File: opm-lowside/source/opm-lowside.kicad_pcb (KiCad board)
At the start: 2 copper layers, 82 parts, among them IC1 INA180A3IDBVR, IC2 INA180A3IDBVR, IC3 INA180A3IDBVR, IC4 TMC6100-LA, J1 Current Sensing, J2 SPI/Info, J3 VCC_IO, J4 PWMx6, J5 Temperature, Q1 HYG025N06LS1C2, Q2 HYG025N06LS1C2, Q3 HYG025N06LS1C2, Q4 HYG025N06LS1C2, Q5 HYG025N06LS1C2, Q6 HYG025N06LS1C2, U1 TerminalBlock_2_P5.08mm, U2 TerminalBlock_3_P5.08mm

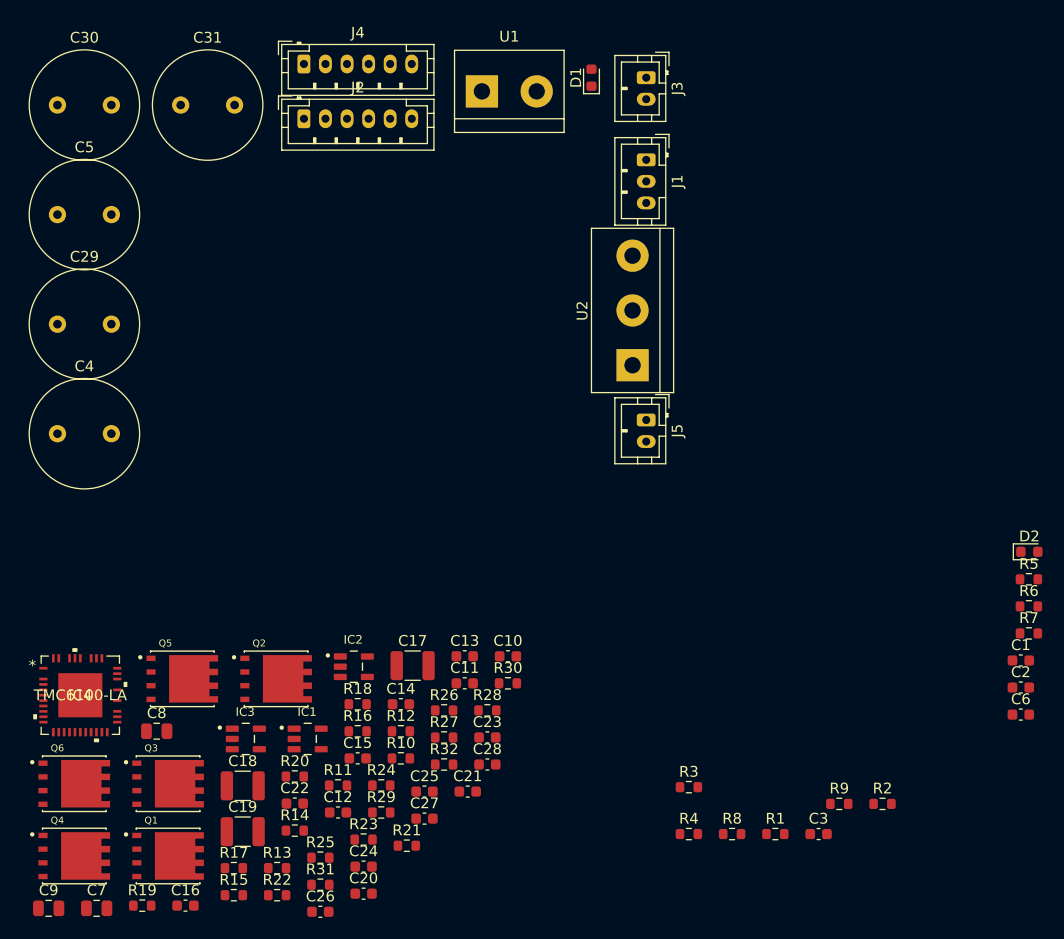
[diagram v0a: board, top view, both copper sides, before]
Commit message: add heatsink
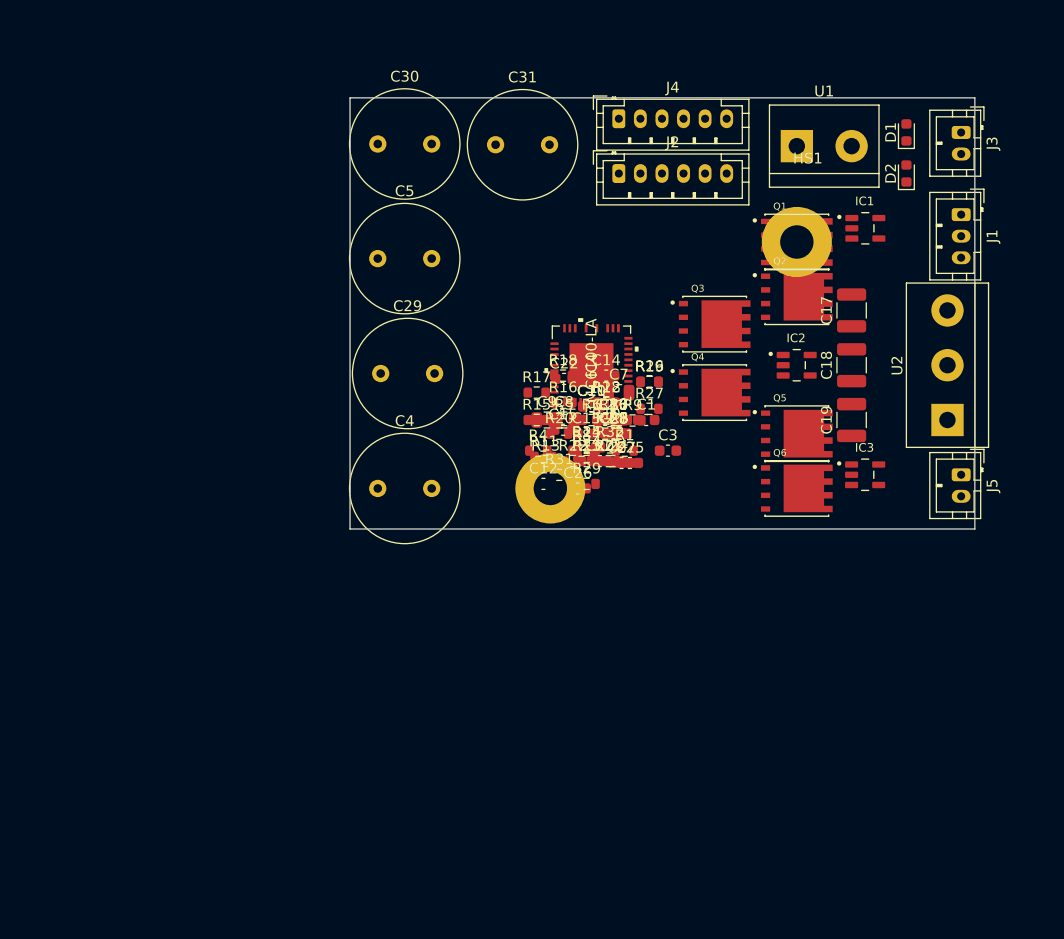
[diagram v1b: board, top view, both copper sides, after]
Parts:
- added HS1: Heatsink, Libraries:Heatsink_30x30mm_2xFixation3mm, F.Cu at (144.8, 106.7)
- moved Q1 81.5 mm to (171.4, 80.0)
- moved Q4 73.3 mm to (163.8, 94.0)
- moved Q6 72.4 mm to (171.4, 102.9)
- moved IC1 70.1 mm to (177.8, 78.7)
- moved C18 68.6 mm to (176.5, 91.4), turned to 90 degrees
- moved C19 68.2 mm to (176.5, 96.5), turned to 90 degrees
- moved C7 68.1 mm to (154.9, 94.0)
- moved R19 67.6 mm to (157.8, 93.0)
- moved Q3 66.2 mm to (163.8, 87.6)
- moved C9 64.7 mm to (148.3, 96.5)
- moved IC3 62.5 mm to (177.8, 101.6)
- moved Q5 61.4 mm to (171.4, 97.8)
- moved C16 60.0 mm to (154.4, 96.5)
- moved Q2 59.9 mm to (171.4, 85.1)
- moved IC4 56.4 mm to (152.4, 91.4), turned to 90 degrees
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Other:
- board outline added: 58 x 40 mm

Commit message: add step
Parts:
- IC4: value TMC6100-LA -> QFN37_7X7_TRI
- moved HS1 73.7 mm to (218.4, 105.4)
- moved C26 37.7 mm to (181.1, 80.0)
- moved C24 35.1 mm to (181.1, 77.5)
- moved R30 32.1 mm to (181.2, 78.7)
- moved C20 31.1 mm to (177.8, 81.3)
- moved C22 30.7 mm to (177.8, 105.4)
- moved R24 29.7 mm to (174.0, 80.0)
- moved R21 29.4 mm to (174.0, 78.7)
- moved R25 29.0 mm to (174.8, 81.3)
- moved R18 28.5 mm to (174.0, 77.5)
- moved C28 27.9 mm to (181.6, 104.1)
- moved R32 27.8 mm to (181.6, 102.9)
- moved C23 27.6 mm to (181.6, 101.6)
- moved R31 26.2 mm to (173.5, 91.4)
- moved R20 24.7 mm to (174.0, 100.3)
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
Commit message: update parts
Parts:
- C17: value 2,2μF/100V -> 2.2μF/100V
- IC4: value QFN37_7X7_TRI -> TMC6100-LA
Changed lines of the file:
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@@
       (effects (font (size 1 1) (thickness 0.15)))
     )
-    (fp_text value 2,2μF/100V (at 0 2.3 90) (layer F.Fab)
+    (fp_text value 2.2μF/100V (at 0 2.3 90) (layer F.Fab)
       (effects (font (size 1 1) (thickness 0.15)))
     )
@@
       (effects (font (size 1 1) (thickness 0.15)))
     )
-    (fp_text value QFN37_7X7_TRI (at 0 0 90) (layer F.SilkS)
-      (effects (font (size 1 1) (thickness 0.15)))
-    )
+    (fp_text value TMC6100-LA (at 0 0 90) (layer F.SilkS)
+      (effects (font (size 1 1) (thickness 0.15)))
+    )

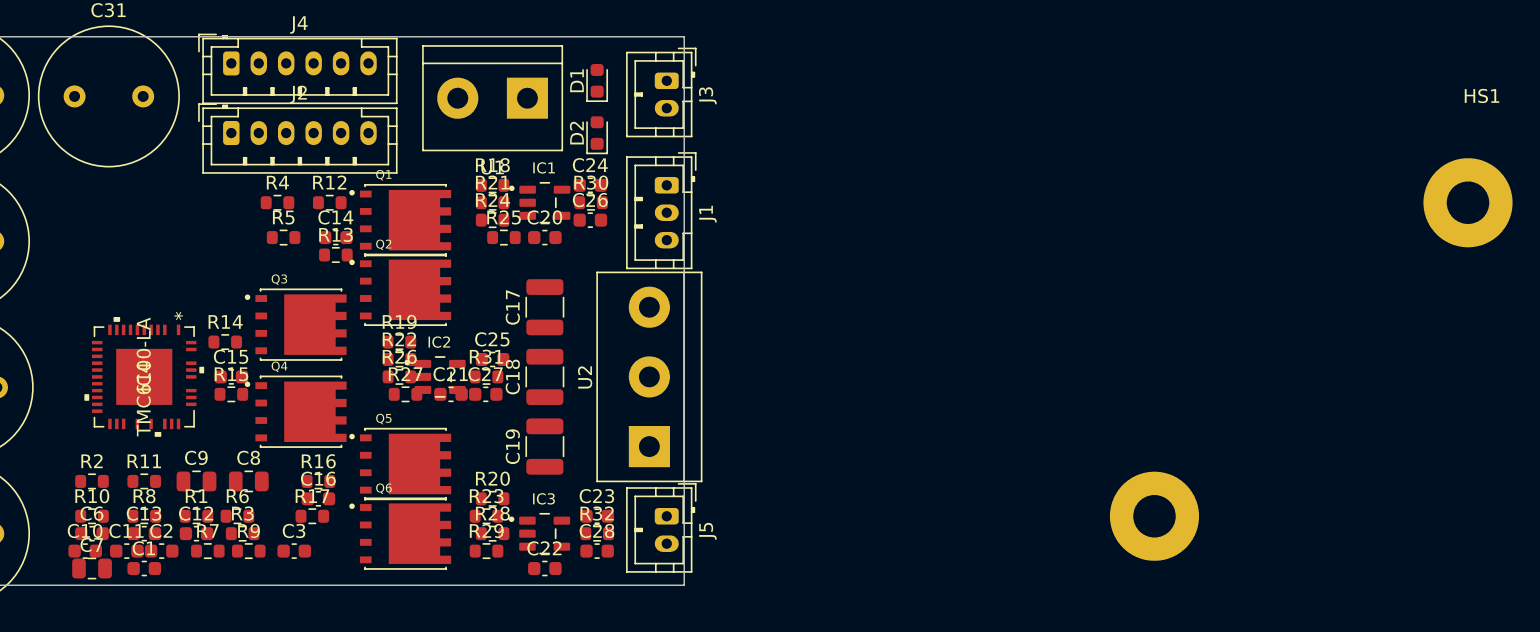
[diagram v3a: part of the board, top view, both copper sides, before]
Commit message: add fan
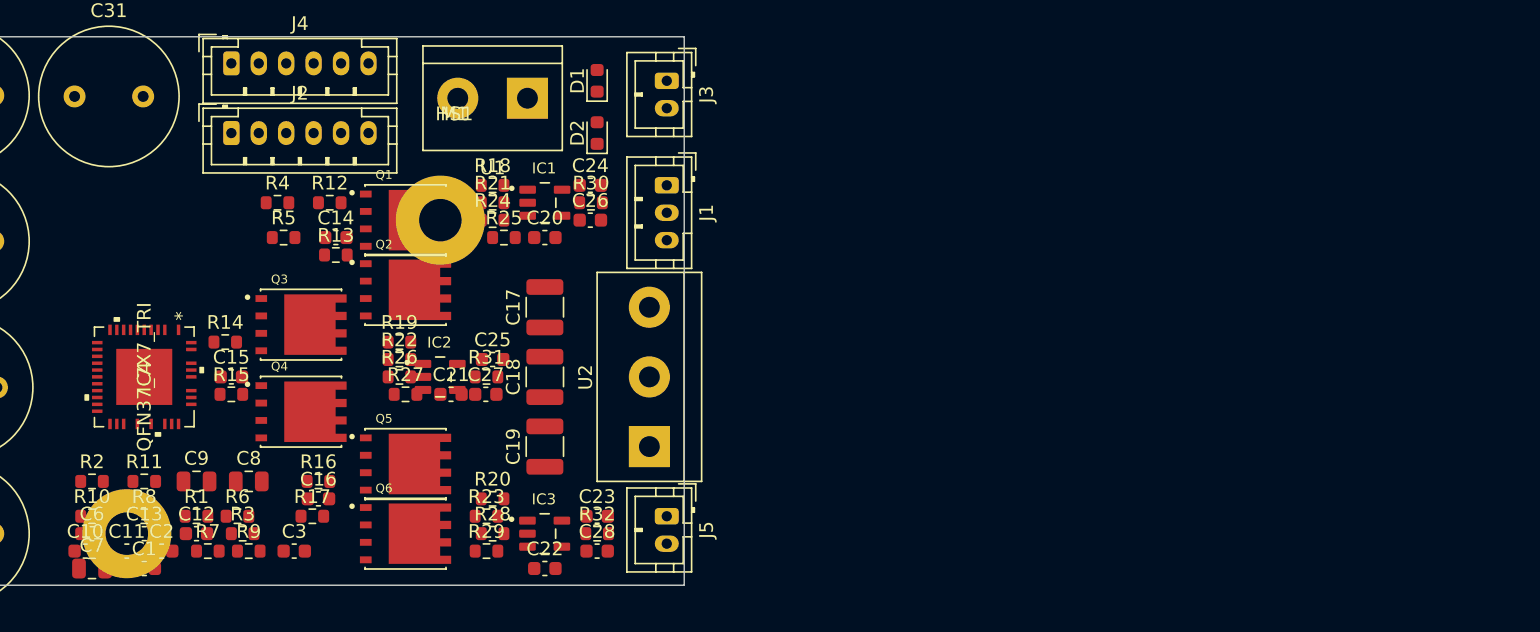
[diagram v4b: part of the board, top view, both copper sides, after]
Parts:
- added M1: Fan, Libraries:Fan_3010, F.Cu at (143.5, 106.7)
- IC4: value TMC6100-LA -> QFN37_7X7_TRI
- moved HS1 74.9 mm to (143.5, 106.7)
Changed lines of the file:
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@@
     (tracks 0)
     (zones 0)
-    (modules 83)
+    (modules 84)
     (nets 83)
   )
@@
       (effects (font (size 1 1) (thickness 0.15)))
     )
-    (fp_text value TMC6100-LA (at 0 0 90) (layer F.SilkS)
+    (fp_text value QFN37_7X7_TRI (at 0 0 90) (layer F.SilkS)
       (effects (font (size 1 1) (thickness 0.15)))
     )
@@
   )
   (module Libraries:Heatsink_30x30mm_2xFixation3mm (layer F.Cu)
-    (at 218.44 105.41)
+    (at 143.51 106.68)
     (descr "Heatsink, 62 x 40mm, 2x 3mm Drills,")
     (tags heatsink)
@@
     )
   )
+  (module Libraries:Fan_3010 (layer F.Cu)
+    (at 143.51 106.68)
+    (descr "fan 3010")
+    (tags heatsink)
+    (fp_text reference M1 (at 27.686 -34.417) (layer F.SilkS)
+      (effects (font (size 1 1) (thickness 0.15)))
+    )
+    (fp_text value Fan (at 11.43 -3.81) (layer F.Fab)
+      (effects (font (size 1 1) (thickness 0.15)))
+    )
+    (fp_arc (start 1.422977 -28.380326) (end 1.422977 -29.880326) (angle -90) (layer Dwgs.User) (width 0.2))
+    (fp_arc (start 1.422977 -1.680326) (end 0.562977 -1.680326) (angle -90) (layer Dwgs.User) (width 0.2))
+    (fp_arc (start 28.122977 -1.680326) (end 28.122977 -0.180326) (angle -90) (layer Dwgs.User) (width 0.2))
+    (fp_arc (start 1.422977 -1.680326) (end -0.077023 -1.680326) (angle -90) (layer Dwgs.User) (width 0.2))
+    (fp_arc (start 28.122977 -1.680326) (end 28.122977 -0.820326) (angle -90) (layer Dwgs.User) (width 0.2))
+    (fp_arc (start 1.422977 -28.380326) (end 1.422977 -29.240326) (angle -90) (layer Dwgs.User) (width 0.2))
+    (fp_arc (start 28.122977 -28.380326) (end 28.982977 -28.380326) (angle -90) (layer Dwgs.User) (width 0.2))
+    (fp_arc (start 28.122977 -28.380326) (end 29.622977 -28.380326) (angle -90) (layer Dwgs.User) (width 0.2))
+    (fp_circle (center 26.67 -3.81) (end 28.095 -3.81) (layer Dwgs.User) (width 0.2))
+    (fp_circle (center 3.272977 -26.67) (end 4.697977 -26.67) (layer Dwgs.User) (width 0.2))
+    (fp_line (start 1.422977 -0.820326) (end 28.122977 -0.820326) (layer Dwgs.User) (width 0.2))
+    (fp_line (start -0.077023 -28.380326) (end -0.077023 -1.680326) (layer Dwgs.User) (width 0.2))
+    (fp_line (start 0.562977 -28.380326) (end 0.562977 -1.680326) (layer Dwgs.User) (width 0.2))
+    (fp_line (start 28.122977 -29.880326) (end 1.422977 -29.880326) (layer Dwgs.User) (width 0.2))
+    (fp_line (start 28.122977 -29.240326) (end 1.422977 -29.240326) (layer Dwgs.User) (width 0.2))
+    (fp_line (start 29.622977 -1.680326) (end 29.622977 -28.380326) (layer Dwgs.User) (width 0.2))
+    (fp_line (start 28.982977 -1.680326) (end 28.982977 -28.380326) (layer Dwgs.User) (width 0.2))
+    (fp_line (start 1.422977 -0.180326) (end 28.122977 -0.180326) (layer Dwgs.User) (width 0.2))
+    (fp_circle (center 3.272977 -3.530326) (end 4.697977 -3.530326) (layer Dwgs.User) (width 0.2))
+    (fp_circle (center 26.272977 -26.530326) (end 27.697977 -26.530326) (layer Dwgs.User) (width 0.2))
+    (model ${KIPRJMOD}/Libraries/Fan3010.step
+      (offset (xyz 20 16 13))
+      (scale (xyz 1 1 1))
+      (rotate (xyz 0 0 0))
+    )
+  )

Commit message: change spacing
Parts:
- moved C29 0.36 mm to (132.6, 92.0)
- moved C4 0.30 mm to (132.6, 102.6)
- moved C30 0.10 mm to (132.6, 71.0)
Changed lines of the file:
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@@
   )
   (module Capacitor_THT:C_Radial_D10.0mm_H20.0mm_P5.00mm (layer F.Cu)
-    (at 132.58 102.87)
+    (at 132.58 102.57)
     (descr "C, Radial series, Radial, pin pitch=5.00mm, diameter=10mm, height=20mm, Non-Polar Electrolytic Capacitor")
     (tags "C Radial series Radial pin pitch 5.00mm diameter 10mm height 20mm Non-Polar Electrolytic Capacitor")
@@
   )
   (module Capacitor_THT:C_Radial_D10.0mm_H20.0mm_P5.00mm (layer F.Cu)
-    (at 132.85 92.21)
+    (at 132.55 92.01)
     (descr "C, Radial series, Radial, pin pitch=5.00mm, diameter=10mm, height=20mm, Non-Polar Electrolytic Capacitor")
     (tags "C Radial series Radial pin pitch 5.00mm diameter 10mm height 20mm Non-Polar Electrolytic Capacitor")
@@
   )
   (module Capacitor_THT:C_Radial_D10.0mm_H20.0mm_P5.00mm (layer F.Cu)
-    (at 132.58 70.92)
+    (at 132.58 71.02)
     (descr "C, Radial series, Radial, pin pitch=5.00mm, diameter=10mm, height=20mm, Non-Polar Electrolytic Capacitor")
     (tags "C Radial series Radial pin pitch 5.00mm diameter 10mm height 20mm Non-Polar Electrolytic Capacitor")

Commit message: increase caps
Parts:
- C17: value 2.2μF/100V -> 10uF/100V; footprint Capacitor_SMD:C_1210_3225Metric -> Capacitor_SMD:C_2220_5650Metric
- C18, C19: value 2,2μF/100V -> 10uF/100V; footprint Capacitor_SMD:C_1210_3225Metric -> Capacitor_SMD:C_2220_5650Metric
- C8, C9: value 2,2μF/50V -> 2,2uF/50V
- IC4: value QFN37_7X7_TRI -> TMC6100-LA
- R10, R11: value 0Ω -> 0R
- R12, R13, R14, R15, R16, R17: value 2,2Ω/1% -> 2.2R/1%
- R18, R19, R20, R21, R22, R23: value .001Ω/1% -> R001/1%
- R24, R25, R26, R27, R28, R29: value 10Ω/1% -> 10R/1%
- R30, R31, R32: value 100Ω/5% -> 100R/5%
- moved HS1 101.4 mm to (237.5, 68.6)
- moved M1 94.1 mm to (237.5, 102.9)
- moved R20 5.08 mm to (174.0, 105.4)
- moved R12 3.81 mm to (158.3, 78.7)
- moved R4 3.81 mm to (154.5, 78.7)
- moved C21 2.85 mm to (168.1, 93.2)
- moved C25 2.85 mm to (171.2, 90.7)
- moved C27 2.85 mm to (170.7, 93.2)
- moved IC2 2.85 mm to (167.4, 91.9)
- moved R19 2.85 mm to (164.4, 89.4)
- moved R22 2.85 mm to (164.4, 90.7)
- moved R26 2.85 mm to (164.4, 91.9)
- moved R27 2.85 mm to (164.8, 93.2)
- moved C2 2.54 mm to (147.3, 104.1)
- moved C8 2.54 mm to (153.7, 99.1)
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
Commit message: update position
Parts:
- IC4: value TMC6100-LA -> QFN37_7X7_TRI
- moved U2 10.2 mm to (175.3, 96.5)
- moved C17 7.63 mm to (184.2, 85.1)
- moved C18 7.62 mm to (184.2, 91.4)
- moved C19 7.62 mm to (184.2, 97.8)
- moved R5 3.29 mm to (159.6, 78.7)
- moved R12 2.84 mm to (160.8, 80.0)
- moved J1 2.54 mm to (186.7, 74.9)
- moved R4 2.16 mm to (156.7, 78.7)
- moved IC2 1.79 mm to (167.6, 90.2)
- moved J5 1.27 mm to (186.7, 102.9)
- moved J3 1.27 mm to (186.7, 68.6)
- moved C14 0.50 mm to (160.8, 81.3)
- moved R13 0.44 mm to (160.8, 82.5)

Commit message: try routing
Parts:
- moved C31 3.50 mm to (146.1, 68.6), turned to 270 degrees
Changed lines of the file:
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@@
   )
   (module Capacitor_THT:C_Radial_D10.0mm_H20.0mm_P5.00mm (layer F.Cu)
-    (at 143.51 70.99)
+    (at 146.05 68.58 270)
     (descr "C, Radial series, Radial, pin pitch=5.00mm, diameter=10mm, height=20mm, Non-Polar Electrolytic Capacitor")
     (tags "C Radial series Radial pin pitch 5.00mm diameter 10mm height 20mm Non-Polar Electrolytic Capacitor")
-    (fp_text reference C31 (at 2.5 -6.25) (layer F.SilkS)
+    (fp_text reference C31 (at 2.5 -6.25 90) (layer F.SilkS)
       (effects (font (size 1 1) (thickness 0.15)))
     )
-    (fp_text value 330uF/63V (at 2.5 6.25) (layer F.Fab)
+    (fp_text value 330uF/63V (at 2.5 6.25 90) (layer F.Fab)
       (effects (font (size 1 1) (thickness 0.15)))
     )
-    (fp_text user %R (at 2.5 0) (layer F.Fab)
+    (fp_text user %R (at 2.5 0 90) (layer F.Fab)
       (effects (font (size 1 1) (thickness 0.15)))
     )
@@
     (fp_circle (center 2.5 0) (end 7.62 0) (layer F.SilkS) (width 0.12))
     (fp_circle (center 2.5 0) (end 7.75 0) (layer F.CrtYd) (width 0.05))
-    (pad 2 thru_hole circle (at 5 0) (size 1.6 1.6) (drill 0.8) (layers *.Cu *.Mask)
+    (pad 2 thru_hole circle (at 5 0 270) (size 1.6 1.6) (drill 0.8) (layers *.Cu *.Mask)
       (net 2 +5V))
-    (pad 1 thru_hole circle (at 0 0) (size 1.6 1.6) (drill 0.8) (layers *.Cu *.Mask)
+    (pad 1 thru_hole circle (at 0 0 270) (size 1.6 1.6) (drill 0.8) (layers *.Cu *.Mask)
       (net 5 /+VM))
     (model ${KISYS3DMOD}/Capacitor_THT.3dshapes/C_Radial_D10.0mm_H20.0mm_P5.00mm.wrl
